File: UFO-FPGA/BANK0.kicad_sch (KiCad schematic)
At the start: 7 parts, among them U1 ICE40HX8K-BG121

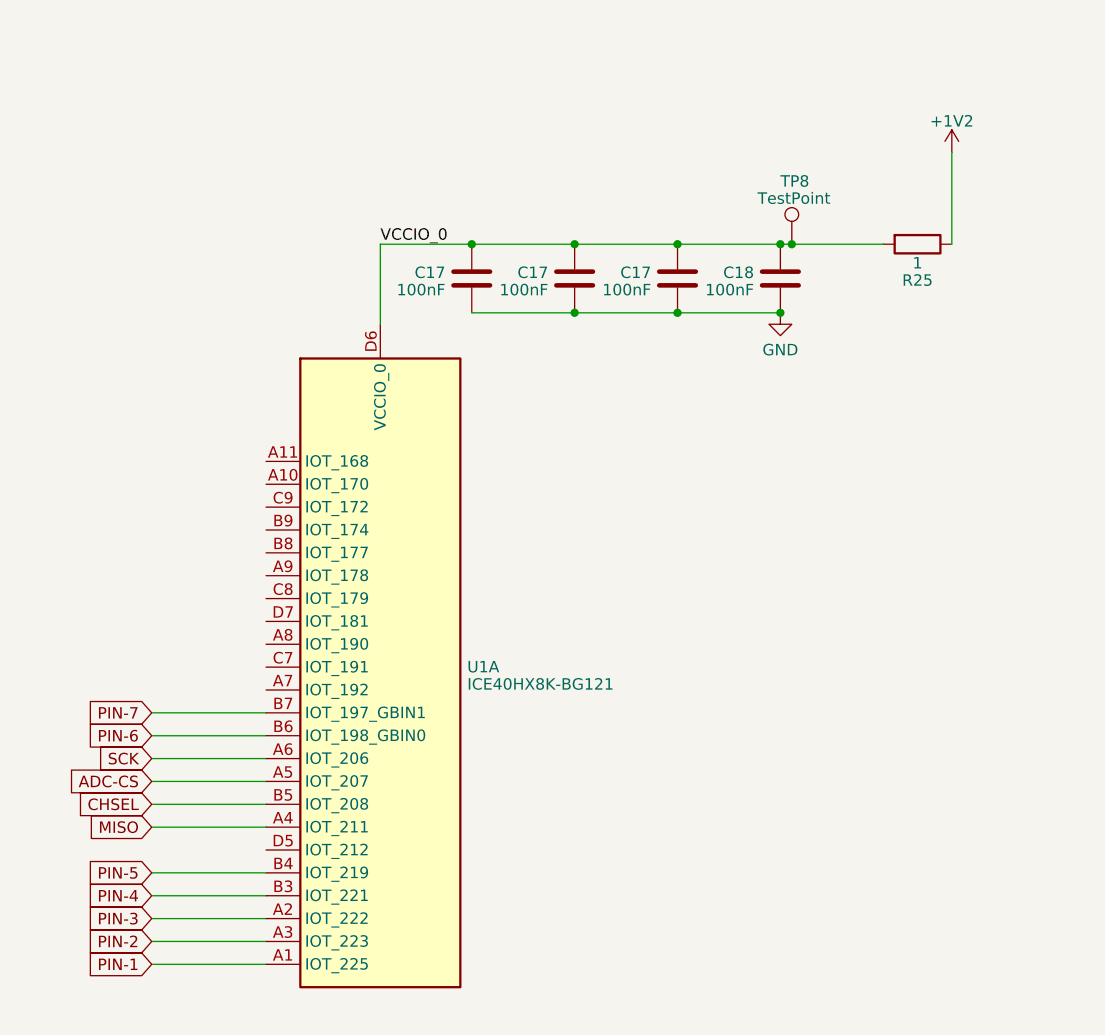
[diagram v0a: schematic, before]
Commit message: Opamp gemaakt van de ADC
Enkel nog begrijpen wat VDC is. Aan docent vragen?
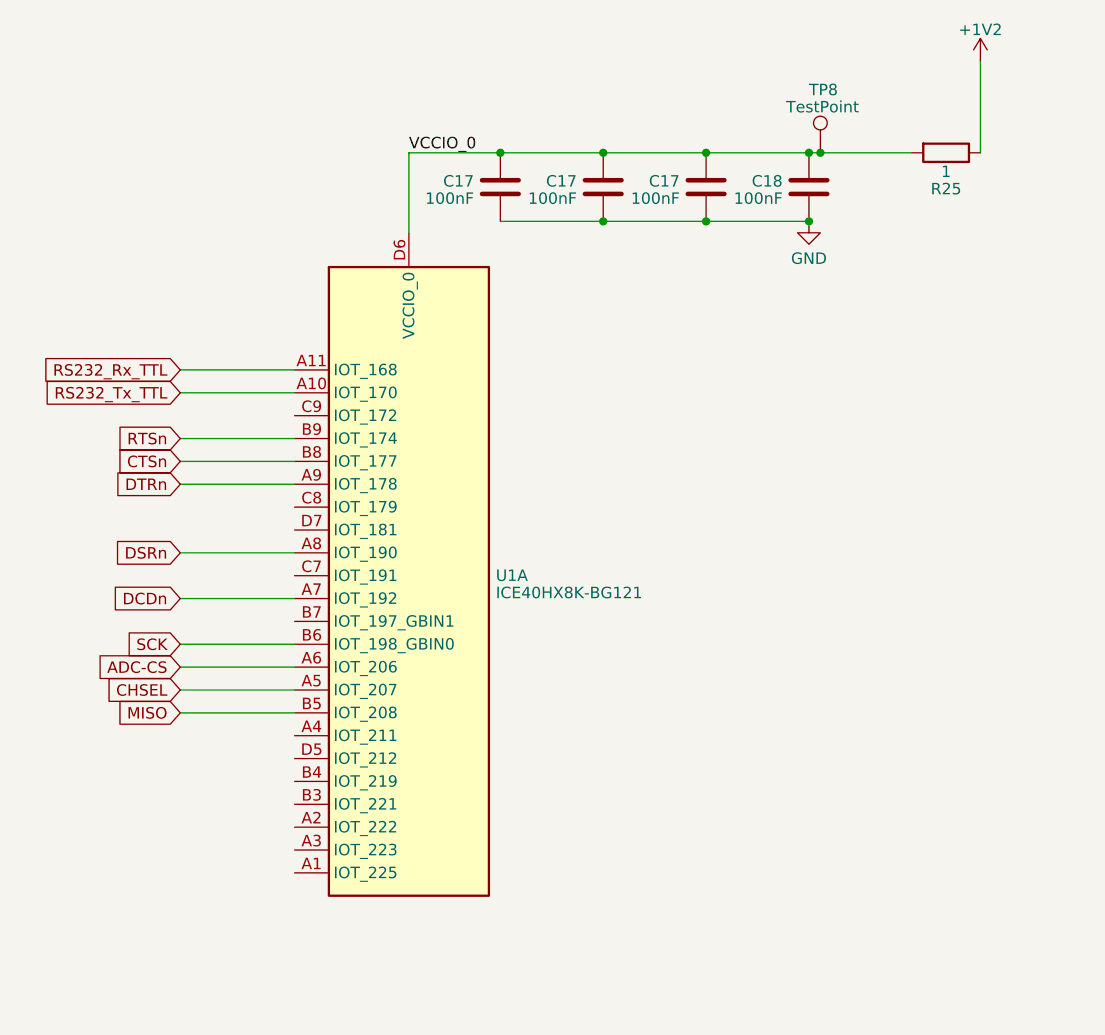
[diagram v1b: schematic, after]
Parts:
- removed C17 (x3): 100nF, symbol Device:C
- added C17 (x3): 100nF, symbol Device:C
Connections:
- net PIN-6 is gone; now on net SCK: U1.B6 (IOT_198_GBIN0)
- net ADC-CS: now also U1.A6 (IOT_206); no longer U1.A5 (IOT_207)
- net CHSEL: now also U1.A5 (IOT_207); no longer U1.B5 (IOT_208)
- net GND: now also C17.2, C17.2, C17.2
- net MISO: now also U1.B5 (IOT_208); no longer U1.A4 (IOT_211)
- net SCK: no longer U1.A6 (IOT_206)
- net VCCIO_0: now also C17.1, C17.1, C17.1
- net RS232_Tx_TTL: now reaches U1.A10 (IOT_170)
- net RS232_Rx_TTL: now reaches U1.A11 (IOT_168)
- net DCDn: now reaches U1.A7 (IOT_192)
- net DSRn: now reaches U1.A8 (IOT_190)
- net DTRn: now reaches U1.A9 (IOT_178)
- net CTSn: now reaches U1.B8 (IOT_177)
- net RTSn: now reaches U1.B9 (IOT_174)
- net PIN-1: no longer names the net of U1.A1 (IOT_225)
- net PIN-2: no longer names the net of U1.A3 (IOT_223)
- net PIN-3: no longer names the net of U1.A2 (IOT_222)
- net PIN-4: no longer names the net of U1.B3 (IOT_221)
- net PIN-5: no longer names the net of U1.B4 (IOT_219)
- net PIN-7: no longer names the net of U1.B7 (IOT_197_GBIN1)

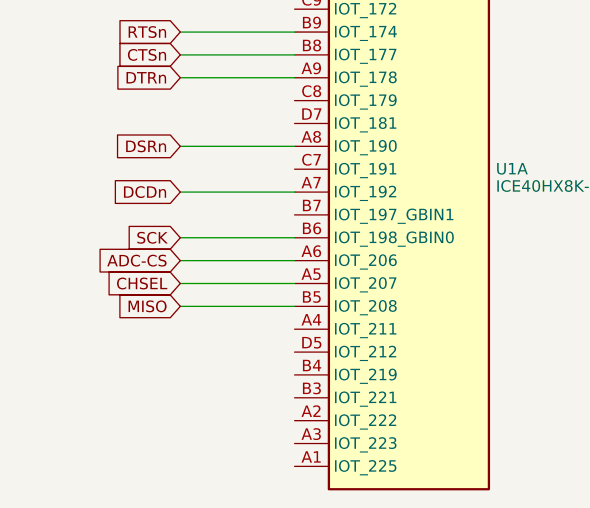
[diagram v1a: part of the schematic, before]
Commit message: pins and USB
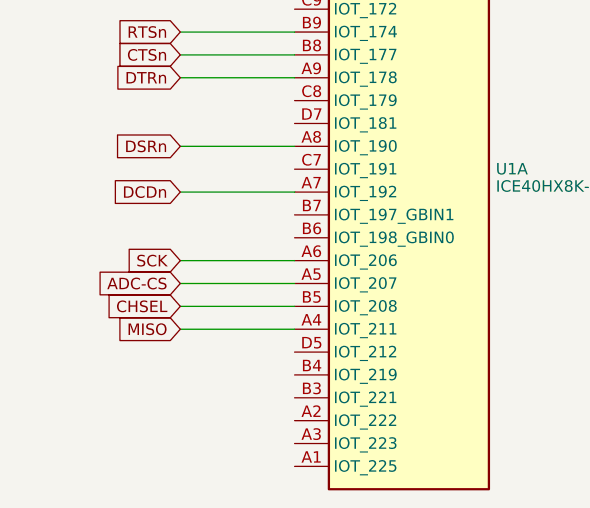
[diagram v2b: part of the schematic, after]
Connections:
- net ADC-CS: now also U1.A5 (IOT_207); no longer U1.A6 (IOT_206)
- net CHSEL: now also U1.B5 (IOT_208); no longer U1.A5 (IOT_207)
- net MISO: now also U1.A4 (IOT_211); no longer U1.B5 (IOT_208)
- net SCK: now also U1.A6 (IOT_206); no longer U1.B6 (IOT_198_GBIN0)
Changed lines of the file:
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@@
     (stroke (width 0) (type default))
   )
-  (wire (pts (xy 92.71 97.79) (xy 105.41 97.79))
+  (wire (pts (xy 92.71 100.33) (xy 105.41 100.33))
     (stroke (width 0) (type default))
   )
@@
     (stroke (width 0) (type default))
   )
-  (wire (pts (xy 92.71 95.25) (xy 105.41 95.25))
+  (wire (pts (xy 92.71 97.79) (xy 105.41 97.79))
     (stroke (width 0) (type default))
   )
@@
     (stroke (width 0) (type default))
   )
-  (wire (pts (xy 92.71 90.17) (xy 105.41 90.17))
+  (wire (pts (xy 92.71 92.71) (xy 105.41 92.71))
     (stroke (width 0) (type default))
   )
@@
     (stroke (width 0) (type default))
   )
-  (wire (pts (xy 92.71 92.71) (xy 105.41 92.71))
+  (wire (pts (xy 92.71 95.25) (xy 105.41 95.25))
     (stroke (width 0) (type default))
   )
@@
     (effects (font (size 1.27 1.27)) (justify left bottom))
   )
-  (global_label "ADC-CS" (shape input) (at 92.71 92.71 180) (fields_autoplaced)
+  (global_label "ADC-CS" (shape input) (at 92.71 95.25 180) (fields_autoplaced)
     (effects (font (size 1.27 1.27)) (justify right))
-    (property "Intersheetrefs" "${INTERSHEET_REFS}" (at 82.1237 92.71 0)
+    (property "Intersheetrefs" "${INTERSHEET_REFS}" (at 82.1237 95.25 0)
       (effects (font (size 1.27 1.27)) (justify right) hide)
     )
@@
     )
   )
-  (global_label "SCK" (shape input) (at 92.71 90.17 180) (fields_autoplaced)
+  (global_label "SCK" (shape input) (at 92.71 92.71 180) (fields_autoplaced)
     (effects (font (size 1.27 1.27)) (justify right))
-    (property "Intersheetrefs" "${INTERSHEET_REFS}" (at 86.0547 90.17 0)
+    (property "Intersheetrefs" "${INTERSHEET_REFS}" (at 86.0547 92.71 0)
       (effects (font (size 1.27 1.27)) (justify right) hide)
     )
@@
     )
   )
-  (global_label "CHSEL" (shape input) (at 92.71 95.25 180) (fields_autoplaced)
+  (global_label "CHSEL" (shape input) (at 92.71 97.79 180) (fields_autoplaced)
     (effects (font (size 1.27 1.27)) (justify right))
-    (property "Intersheetrefs" "${INTERSHEET_REFS}" (at 83.8171 95.25 0)
+    (property "Intersheetrefs" "${INTERSHEET_REFS}" (at 83.8171 97.79 0)
       (effects (font (size 1.27 1.27)) (justify right) hide)
     )
   )
-  (global_label "MISO" (shape input) (at 92.71 97.79 180) (fields_autoplaced)
+  (global_label "MISO" (shape input) (at 92.71 100.33 180) (fields_autoplaced)
     (effects (font (size 1.27 1.27)) (justify right))
-    (property "Intersheetrefs" "${INTERSHEET_REFS}" (at 85.208 97.79 0)
+    (property "Intersheetrefs" "${INTERSHEET_REFS}" (at 85.208 100.33 0)
       (effects (font (size 1.27 1.27)) (justify right) hide)
     )

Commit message: De inverting supply schakeling gemaakt
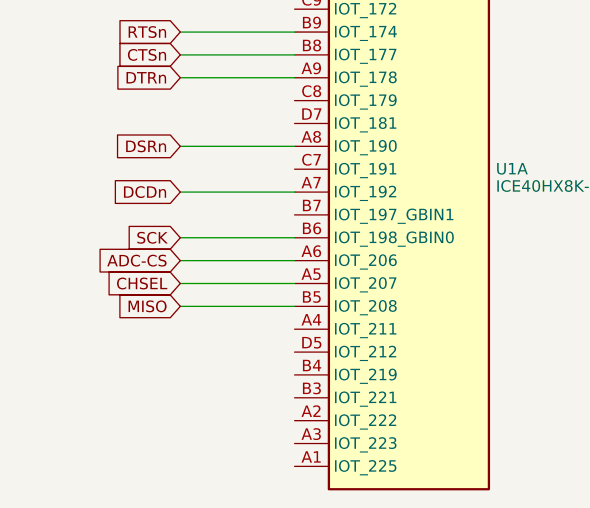
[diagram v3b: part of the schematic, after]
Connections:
- net ADC-CS: now also U1.A6 (IOT_206); no longer U1.A5 (IOT_207)
- net CHSEL: now also U1.A5 (IOT_207); no longer U1.B5 (IOT_208)
- net MISO: now also U1.B5 (IOT_208); no longer U1.A4 (IOT_211)
- net SCK: now also U1.B6 (IOT_198_GBIN0); no longer U1.A6 (IOT_206)
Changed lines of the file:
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@@
     (stroke (width 0) (type default))
   )
-  (wire (pts (xy 92.71 100.33) (xy 105.41 100.33))
+  (wire (pts (xy 92.71 97.79) (xy 105.41 97.79))
     (stroke (width 0) (type default))
   )
@@
     (stroke (width 0) (type default))
   )
-  (wire (pts (xy 92.71 97.79) (xy 105.41 97.79))
+  (wire (pts (xy 92.71 95.25) (xy 105.41 95.25))
     (stroke (width 0) (type default))
   )
@@
     (stroke (width 0) (type default))
   )
-  (wire (pts (xy 92.71 92.71) (xy 105.41 92.71))
+  (wire (pts (xy 92.71 90.17) (xy 105.41 90.17))
     (stroke (width 0) (type default))
   )
@@
     (stroke (width 0) (type default))
   )
-  (wire (pts (xy 92.71 95.25) (xy 105.41 95.25))
+  (wire (pts (xy 92.71 92.71) (xy 105.41 92.71))
     (stroke (width 0) (type default))
   )
@@
     (effects (font (size 1.27 1.27)) (justify left bottom))
   )
-  (global_label "ADC-CS" (shape input) (at 92.71 95.25 180) (fields_autoplaced)
+  (global_label "ADC-CS" (shape input) (at 92.71 92.71 180) (fields_autoplaced)
     (effects (font (size 1.27 1.27)) (justify right))
-    (property "Intersheetrefs" "${INTERSHEET_REFS}" (at 82.1237 95.25 0)
+    (property "Intersheetrefs" "${INTERSHEET_REFS}" (at 82.1237 92.71 0)
       (effects (font (size 1.27 1.27)) (justify right) hide)
     )
@@
     )
   )
-  (global_label "SCK" (shape input) (at 92.71 92.71 180) (fields_autoplaced)
+  (global_label "SCK" (shape input) (at 92.71 90.17 180) (fields_autoplaced)
     (effects (font (size 1.27 1.27)) (justify right))
-    (property "Intersheetrefs" "${INTERSHEET_REFS}" (at 86.0547 92.71 0)
+    (property "Intersheetrefs" "${INTERSHEET_REFS}" (at 86.0547 90.17 0)
       (effects (font (size 1.27 1.27)) (justify right) hide)
     )
@@
     )
   )
-  (global_label "CHSEL" (shape input) (at 92.71 97.79 180) (fields_autoplaced)
+  (global_label "CHSEL" (shape input) (at 92.71 95.25 180) (fields_autoplaced)
     (effects (font (size 1.27 1.27)) (justify right))
-    (property "Intersheetrefs" "${INTERSHEET_REFS}" (at 83.8171 97.79 0)
+    (property "Intersheetrefs" "${INTERSHEET_REFS}" (at 83.8171 95.25 0)
       (effects (font (size 1.27 1.27)) (justify right) hide)
     )
   )
-  (global_label "MISO" (shape input) (at 92.71 100.33 180) (fields_autoplaced)
+  (global_label "MISO" (shape input) (at 92.71 97.79 180) (fields_autoplaced)
     (effects (font (size 1.27 1.27)) (justify right))
-    (property "Intersheetrefs" "${INTERSHEET_REFS}" (at 85.208 100.33 0)
+    (property "Intersheetrefs" "${INTERSHEET_REFS}" (at 85.208 97.79 0)
       (effects (font (size 1.27 1.27)) (justify right) hide)
     )

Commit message: IO and power
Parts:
- removed C17 (x3): 100nF, symbol Device:C
- added C17 (x3): 100nF, symbol Device:C
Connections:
- net ADC-CS: now also U1.A5 (IOT_207); no longer U1.A6 (IOT_206)
- net CHSEL: now also U1.B5 (IOT_208); no longer U1.A5 (IOT_207)
- net GND: now also C17.2, C17.2, C17.2
- net MISO: now also U1.A4 (IOT_211); no longer U1.B5 (IOT_208)
- net SCK: now also U1.A6 (IOT_206); no longer U1.B6 (IOT_198_GBIN0)
- net VCCIO_0: now also C17.1, C17.1, C17.1
- net PIN-1: now reaches U1.A1 (IOT_225)
- net PIN-3: now reaches U1.A2 (IOT_222)
- net PIN-2: now reaches U1.A3 (IOT_223)
- net PIN-4: now reaches U1.B3 (IOT_221)
- net PIN-5: now reaches U1.B4 (IOT_219)
- net PIN-7: now reaches U1.B7 (IOT_197_GBIN1)
- net CTSn: no longer names the net of U1.B8 (IOT_177)
- net DCDn: no longer names the net of U1.A7 (IOT_192)
- net DSRn: no longer names the net of U1.A8 (IOT_190)
- net DTRn: no longer names the net of U1.A9 (IOT_178)
- net RS232_Rx_TTL: no longer names the net of U1.A11 (IOT_168)
- net RS232_Tx_TTL: no longer names the net of U1.A10 (IOT_170)
- net RTSn: no longer names the net of U1.B9 (IOT_174)
- new net PIN-6: U1.B6 (IOT_198_GBIN0)

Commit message: Revision
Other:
- company: (none) -> Universal-Field-Objects
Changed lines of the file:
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@@
   (paper "A4")
   (title_block
-    (date "2023-04-22")
-    (rev "V0.1")
+    (date "2023-04-25")
+    (rev "V0.5")
+    (company "Universal-Field-Objects")
   )
   (junction (at 160.02 48.895) (diameter 0) (color 0 0 0 0)

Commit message: footprints and PCB
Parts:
- R25: footprint (none) -> Resistor_SMD:R_0805_2012Metric_Pad1.20x1.40mm_HandSolder
- TP8: footprint (none) -> TestPoint:TestPoint_Keystone_5000-5004_Miniature
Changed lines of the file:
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@@
       (effects (font (size 1.27 1.27)) (justify left))
     )
-    (property "Footprint" "" (at 177.8 48.895 0)
+    (property "Footprint" "TestPoint:TestPoint_Keystone_5000-5004_Miniature" (at 177.8 48.895 0)
       (effects (font (size 1.27 1.27)) hide)
     )
@@
       (effects (font (size 1.27 1.27)))
     )
-    (property "Footprint" "" (at 186.69 47.117 90)
+    (property "Footprint" "Resistor_SMD:R_0805_2012Metric_Pad1.20x1.40mm_HandSolder" (at 186.69 47.117 90)
       (effects (font (size 1.27 1.27)) hide)
     )

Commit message: footprint
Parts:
- C17, C18: footprint (none) -> Capacitor_SMD:C_0805_2012Metric_Pad1.18x1.45mm_HandSolder
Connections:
- net CHSEL: no longer names the net of U1.B5 (IOT_208)
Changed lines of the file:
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@@
-    (stroke (width 0) (type default))
-  )
-  (wire (pts (xy 101.6 111.125) (xy 114.3 111.125))
     (stroke (width 0) (type default))
   )
@@
     )
   )
-  (global_label "CHSEL" (shape input) (at 101.6 111.125 180) (fields_autoplaced)
-    (effects (font (size 1.27 1.27)) (justify right))
-    (property "Intersheetrefs" "${INTERSHEET_REFS}" (at 92.7071 111.125 0)
-      (effects (font (size 1.27 1.27)) (justify right) hide)
-    )
-  )
   (global_label "PIN-2" (shape input) (at 101.6 126.365 180) (fields_autoplaced)
     (effects (font (size 1.27 1.27)) (justify right))
@@
       (effects (font (size 1.27 1.27)) (justify left))
     )
-    (property "Footprint" "" (at 147.6248 56.515 0)
+    (property "Footprint" "Capacitor_SMD:C_0805_2012Metric_Pad1.18x1.45mm_HandSolder" (at 147.6248 56.515 0)
       (effects (font (size 1.27 1.27)) hide)
     )
@@
       (effects (font (size 1.27 1.27)) (justify left))
     )
-    (property "Footprint" "" (at 159.0548 56.515 0)
+    (property "Footprint" "Capacitor_SMD:C_0805_2012Metric_Pad1.18x1.45mm_HandSolder" (at 159.0548 56.515 0)
       (effects (font (size 1.27 1.27)) hide)
     )
@@
       (effects (font (size 1.27 1.27)) (justify left))
     )
-    (property "Footprint" "" (at 170.4848 56.515 0)
+    (property "Footprint" "Capacitor_SMD:C_0805_2012Metric_Pad1.18x1.45mm_HandSolder" (at 170.4848 56.515 0)
       (effects (font (size 1.27 1.27)) hide)
     )
@@
       (effects (font (size 1.27 1.27)) (justify left))
     )
-    (property "Footprint" "" (at 136.1948 56.515 0)
-      (effects (font (size 1.27 1.27)) hide)
-    )
+    (property "Footprint" "Capacitor_SMD:C_0805_2012Metric_Pad1.18x1.45mm_HandSolder" (at 136.1948 56.515 0)
+      (effects (font (size 1.27 1.27)) hide)
+    )

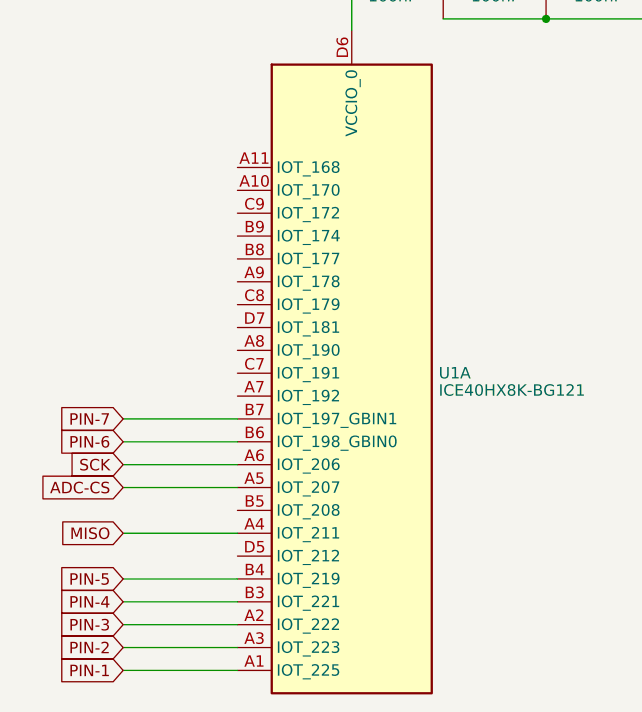
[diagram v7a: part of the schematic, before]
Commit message: PCB planes
Added:
added Power plane +1v2, +3v3 and +5v on layer 4
Ground plane on layer 2 and 5
Added signal layer 1,3 and 6
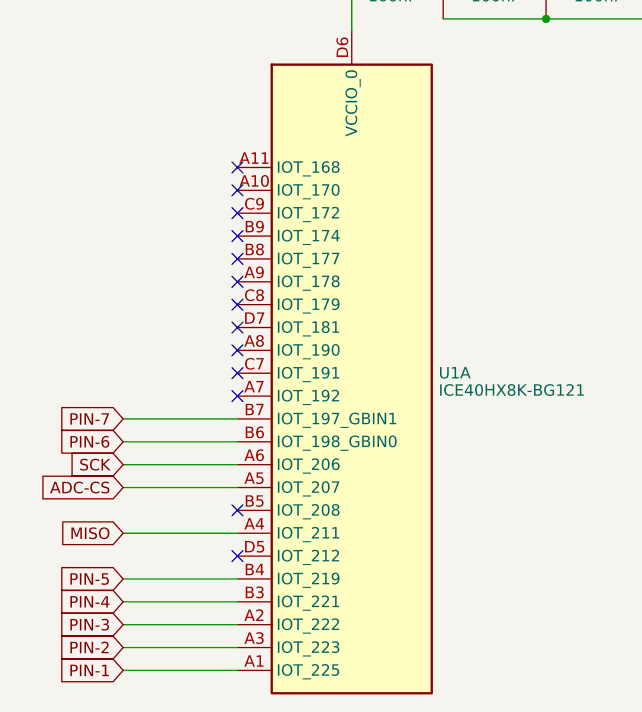
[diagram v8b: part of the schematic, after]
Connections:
- no-connect marks 0 -> 13
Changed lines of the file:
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@@
   (junction (at 148.59 56.515) (diameter 0) (color 0 0 0 0)
   )
+  (no_connect (at 114.3 90.805))
+  (no_connect (at 114.3 85.725))
+  (no_connect (at 114.3 111.125))
+  (no_connect (at 114.3 93.345))
+  (no_connect (at 114.3 78.105))
+  (no_connect (at 114.3 98.425))
+  (no_connect (at 114.3 73.025))
+  (no_connect (at 114.3 75.565))
+  (no_connect (at 114.3 80.645))
+  (no_connect (at 114.3 83.185))
+  (no_connect (at 114.3 116.205))
+  (no_connect (at 114.3 95.885))
+  (no_connect (at 114.3 88.265))
   (wire (pts (xy 101.6 118.745) (xy 114.3 118.745))
     (stroke (width 0) (type default))
